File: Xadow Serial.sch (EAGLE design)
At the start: 28 parts, among them J1 CONNECTOR-HEADER-8P-3461050P1, J2 12p 0.5mm bottom contact, J3 12p 0.5mm bottom contact, J4 12p 0.5mm bottom contact, U1 SC16IS750, U2 BSS138PS, X1 CTS_32X25_SMD

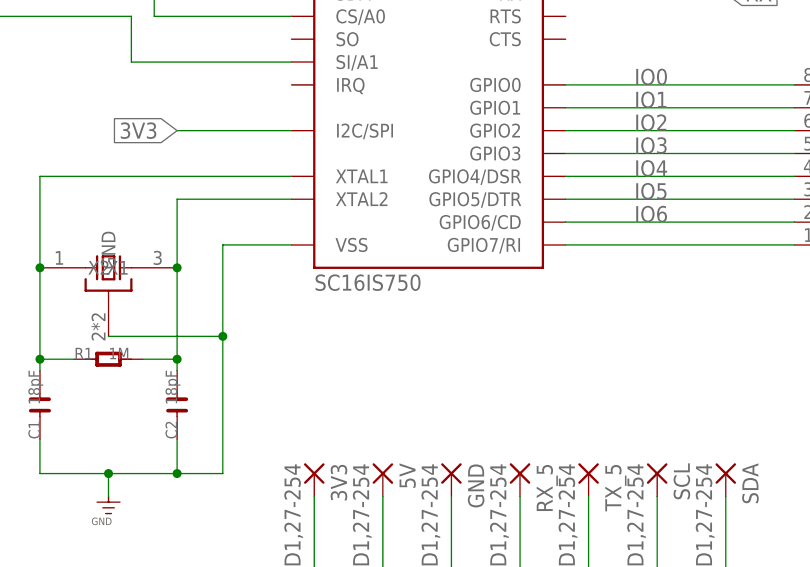
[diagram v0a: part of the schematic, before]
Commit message: Switched to cheaper QFN package
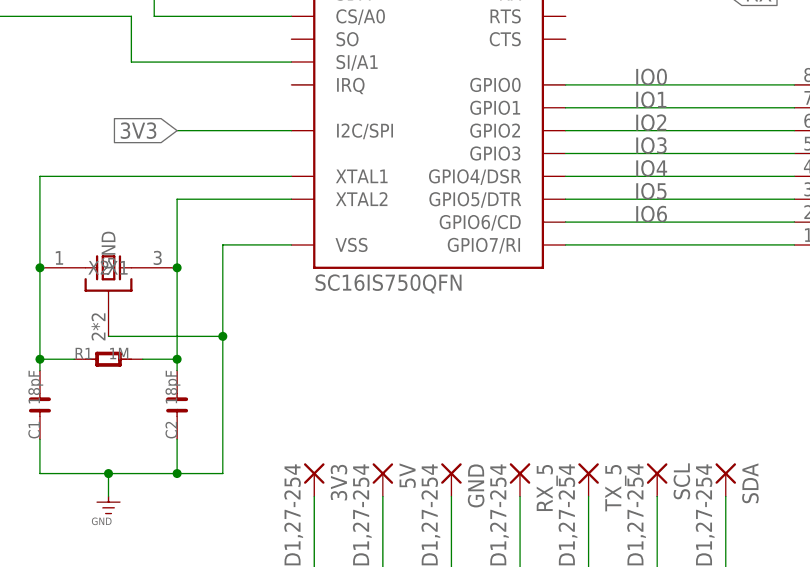
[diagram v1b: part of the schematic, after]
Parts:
- U1: value SC16IS750 -> SC16IS750QFN; device nxpsemi:SC16IS750 -> nxpsemi:SC16IS750QFN
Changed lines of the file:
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@@
 <grid distance="0.1" unitdist="inch" unit="inch" style="lines" multiple="1" display="no" altdistance="0.01" altunitdist="inch" altunit="inch"/>
 <layers>
-<layer number="1" name="Top" color="4" fill="1" visible="no" active="no"/>
-<layer number="2" name="Route2" color="1" fill="3" visible="no" active="no"/>
-<layer number="3" name="Route3" color="4" fill="3" visible="no" active="no"/>
-<layer number="4" name="Route4" color="1" fill="4" visible="no" active="no"/>
-<layer number="5" name="Route5" color="4" fill="4" visible="no" active="no"/>
-<layer number="6" name="Route6" color="1" fill="8" visible="no" active="no"/>
-<layer number="7" name="Route7" color="4" fill="8" visible="no" active="no"/>
-<layer number="8" name="Route8" color="1" fill="2" visible="no" active="no"/>
-<layer number="9" name="Route9" color="4" fill="2" visible="no" active="no"/>
-<layer number="10" name="Route10" color="1" fill="7" visible="no" active="no"/>
-<layer number="11" name="Route11" color="4" fill="7" visible="no" active="no"/>
-<layer number="12" name="Route12" color="1" fill="5" visible="no" active="no"/>
-<layer number="13" name="Route13" color="4" fill="5" visible="no" active="no"/>
-<layer number="14" name="Route14" color="1" fill="6" visible="no" active="no"/>
-<layer number="15" name="Route15" color="4" fill="6" visible="no" active="no"/>
-<layer number="16" name="Bottom" color="1" fill="1" visible="no" active="no"/>
-<layer number="17" name="Pads" color="2" fill="1" visible="no" active="no"/>
-<layer number="18" name="Vias" color="2" fill="1" visible="no" active="no"/>
-<layer number="19" name="Unrouted" color="6" fill="1" visible="no" active="no"/>
-<layer number="20" name="Dimension" color="5" fill="1" visible="no" active="no"/>
-<layer number="21" name="tPlace" color="7" fill="1" visible="no" active="no"/>
-<layer number="22" name="bPlace" color="3" fill="1" visible="no" active="no"/>
-<layer number="23" name="tOrigins" color="15" fill="1" visible="no" active="no"/>
-<layer number="24" name="bOrigins" color="3" fill="1" visible="no" active="no"/>
-<layer number="25" name="tNames" color="7" fill="1" visible="no" active="no"/>
-<layer number="26" name="bNames" color="3" fill="1" visible="no" active="no"/>
-<layer number="27" name="tValues" color="7" fill="1" visible="no" active="no"/>
-<layer number="28" name="bValues" color="7" fill="1" visible="no" active="no"/>
+<layer number="1" name="Top" color="4" fill="1" visible="yes" active="no"/>
+<layer number="2" name="Route2" color="4" fill="3" visible="yes" active="no"/>
+<layer number="3" name="Route3" color="4" fill="3" visible="yes" active="no"/>
+<layer number="4" name="Route4" color="1" fill="4" visible="yes" active="no"/>
+<layer number="5" name="Route5" color="4" fill="4" visible="yes" active="no"/>
+<layer number="6" name="Route6" color="1" fill="8" visible="yes" active="no"/>
+<layer number="7" name="Route7" color="4" fill="8" visible="yes" active="no"/>
+<layer number="8" name="Route8" color="1" fill="2" visible="yes" active="no"/>
+<layer number="9" name="Route9" color="4" fill="2" visible="yes" active="no"/>
+<layer number="10" name="Route10" color="1" fill="7" visible="yes" active="no"/>
+<layer number="11" name="Route11" color="4" fill="7" visible="yes" active="no"/>
+<layer number="12" name="Route12" color="1" fill="5" visible="yes" active="no"/>
+<layer number="13" name="Route13" color="4" fill="5" visible="yes" active="no"/>
+<layer number="14" name="Route14" color="1" fill="6" visible="yes" active="no"/>
+<layer number="15" name="Route15" color="1" fill="6" visible="yes" active="no"/>
+<layer number="16" name="Bottom" color="1" fill="1" visible="yes" active="no"/>
+<layer number="17" name="Pads" color="2" fill="1" visible="yes" active="no"/>
+<layer number="18" name="Vias" color="2" fill="1" visible="yes" active="no"/>
+<layer number="19" name="Unrouted" color="6" fill="1" visible="yes" active="no"/>
+<layer number="20" name="Dimension" color="5" fill="1" visible="yes" active="no"/>
+<layer number="21" name="tPlace" color="7" fill="1" visible="yes" active="no"/>
+<layer number="22" name="bPlace" color="3" fill="1" visible="yes" active="no"/>
+<layer number="23" name="tOrigins" color="15" fill="1" visible="yes" active="no"/>
+<layer number="24" name="bOrigins" color="3" fill="1" visible="yes" active="no"/>
+<layer number="25" name="tNames" color="7" fill="1" visible="yes" active="no"/>
+<layer number="26" name="bNames" color="3" fill="1" visible="yes" active="no"/>
+<layer number="27" name="tValues" color="7" fill="1" visible="yes" active="no"/>
+<layer number="28" name="bValues" color="7" fill="1" visible="yes" active="no"/>
 <layer number="29" name="tStop" color="7" fill="3" visible="no" active="no"/>
 <layer number="30" name="bStop" color="7" fill="6" visible="no" active="no"/>
@@
 <layer number="35" name="tGlue" color="7" fill="4" visible="no" active="no"/>
 <layer number="36" name="bGlue" color="7" fill="5" visible="no" active="no"/>
-<layer number="37" name="tTest" color="7" fill="1" visible="no" active="no"/>
-<layer number="38" name="bTest" color="7" fill="1" visible="no" active="no"/>
+<layer number="37" name="tTest" color="7" fill="1" visible="yes" active="no"/>
+<layer number="38" name="bTest" color="7" fill="1" visible="yes" active="no"/>
 <layer number="39" name="tKeepout" color="4" fill="11" visible="no" active="no"/>
 <layer number="40" name="bKeepout" color="1" fill="11" visible="no" active="no"/>
@@
 <layer number="44" name="Drills" color="7" fill="1" visible="no" active="no"/>
 <layer number="45" name="Holes" color="7" fill="1" visible="no" active="no"/>
-<layer number="46" name="Milling" color="3" fill="1" visible="no" active="no"/>
-<layer number="47" name="Measures" color="7" fill="1" visible="no" active="no"/>
-<layer number="48" name="Document" color="7" fill="1" visible="no" active="no"/>
-<layer number="49" name="Reference" color="7" fill="1" visible="no" active="no"/>
-<layer number="50" name="dxf" color="7" fill="1" visible="no" active="no"/>
-<layer number="51" name="tDocu" color="7" fill="1" visible="no" active="no"/>
-<layer number="52" name="bDocu" color="7" fill="1" visible="no" active="no"/>
-<layer number="53" name="tGND_GNDA" color="7" fill="9" visible="no" active="no"/>
-<layer number="54" name="bGND_GNDA" color="1" fill="9" visible="no" active="no"/>
-<layer number="56" name="wert" color="7" fill="1" visible="no" active="no"/>
-<layer number="57" name="tCAD" color="7" fill="1" visible="no" active="no"/>
+<layer number="46" name="Milling" color="3" fill="1" visible="yes" active="no"/>
+<layer number="47" name="Measures" color="7" fill="1" visible="yes" active="no"/>
+<layer number="48" name="Document" color="7" fill="1" visible="yes" active="no"/>
+<layer number="49" name="Reference" color="7" fill="1" visible="yes" active="no"/>
+<layer number="50" name="dxf" color="7" fill="1" visible="yes" active="no"/>
+<layer number="51" name="tDocu" color="7" fill="1" visible="yes" active="no"/>
+<layer number="52" name="bDocu" color="7" fill="1" visible="yes" active="no"/>
+<layer number="53" name="tGND_GNDA" color="7" fill="9" visible="yes" active="no"/>
+<layer number="54" name="bGND_GNDA" color="1" fill="9" visible="yes" active="no"/>
+<layer number="56" name="wert" color="7" fill="1" visible="yes" active="no"/>
+<layer number="57" name="tCAD" color="7" fill="1" visible="yes" active="no"/>
 <layer number="90" name="Modules" color="5" fill="1" visible="yes" active="yes"/>
 <layer number="91" name="Nets" color="2" fill="1" visible="yes" active="yes"/>
@@
 <part name="J3" library="template" deviceset="FPC052002-12LT" device="" value="12p 0.5mm bottom contact"/>
 <part name="U$1" library="moudle" deviceset="SEEEDSTUDIO_SCH_FRAME" device=""/>
-<part name="U1" library="nxpsemi" deviceset="SC16IS750" device=""/>
+<part name="U1" library="nxpsemi" deviceset="SC16IS750" device="QFN"/>
 <part name="X1" library="cts_crystal" deviceset="CTS_32X25_SMD" device=""/>
 <part name="C1" library="OPL" deviceset="C*" device="-0603" value="18pF"/>
